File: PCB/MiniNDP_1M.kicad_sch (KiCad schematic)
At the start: 18 parts, among them J1 Conn_02x20_Odd_Even, U1 HC161, U2 HC161, U3 HC161, U4 HC138, U5 FCT821, U6 AS6C8008_TSOPII, U7 1G32

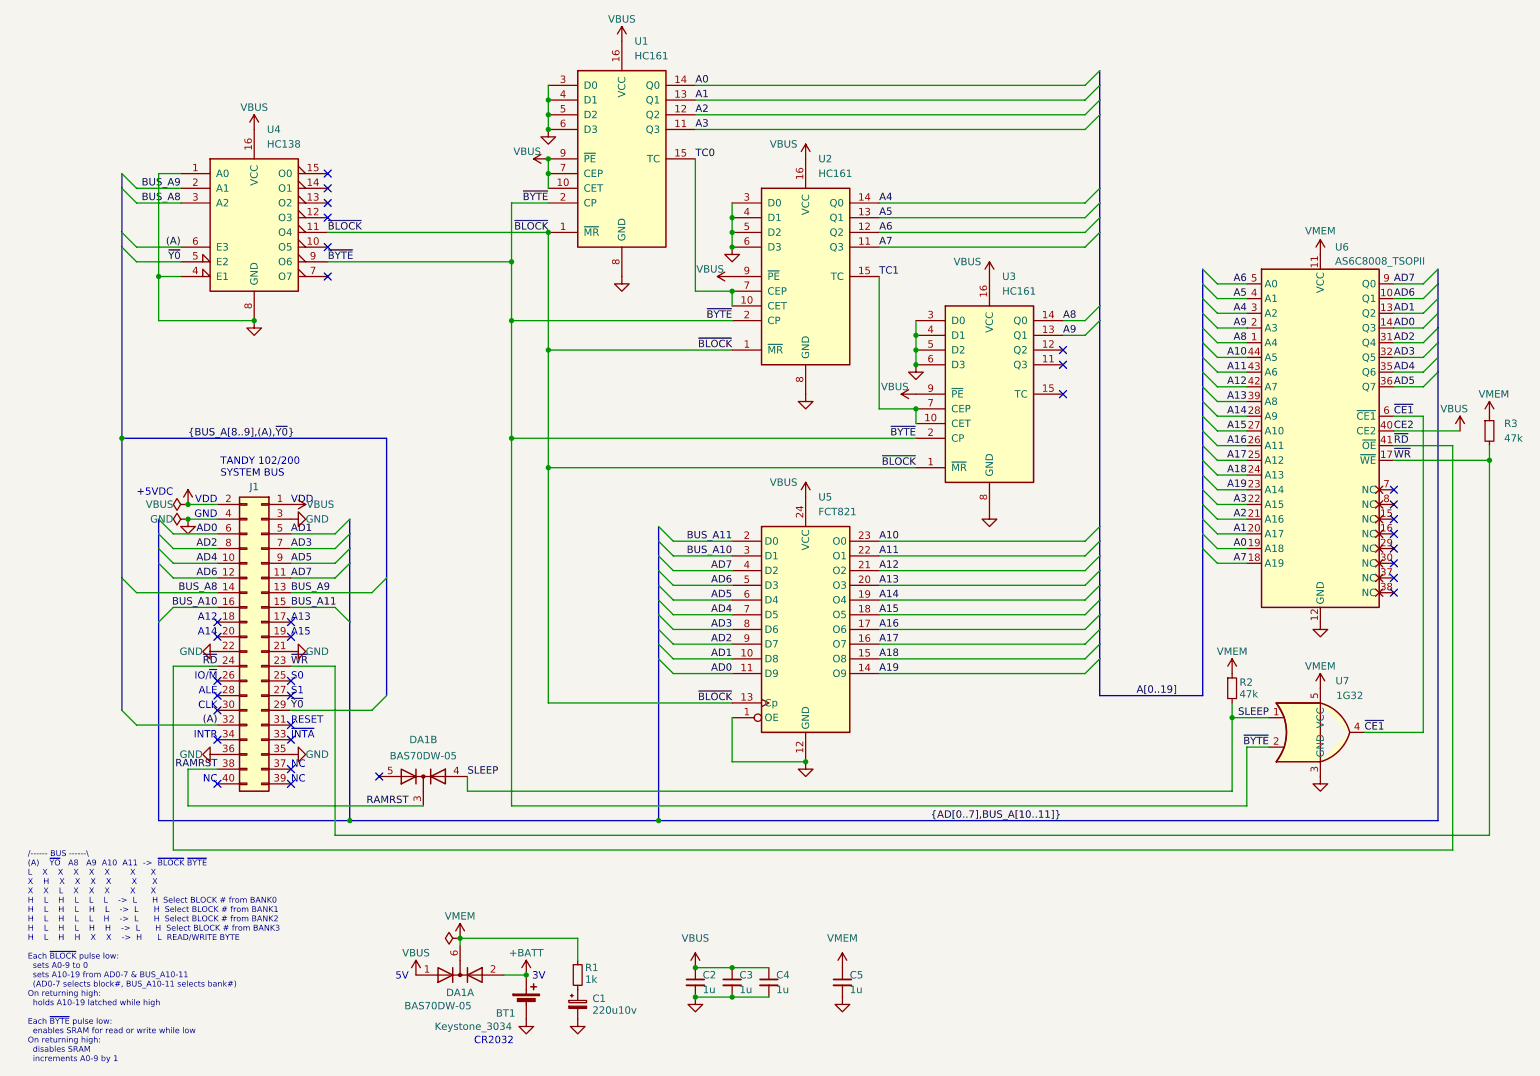
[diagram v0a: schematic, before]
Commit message: Add pullup on /WR. Tighter cover fit.
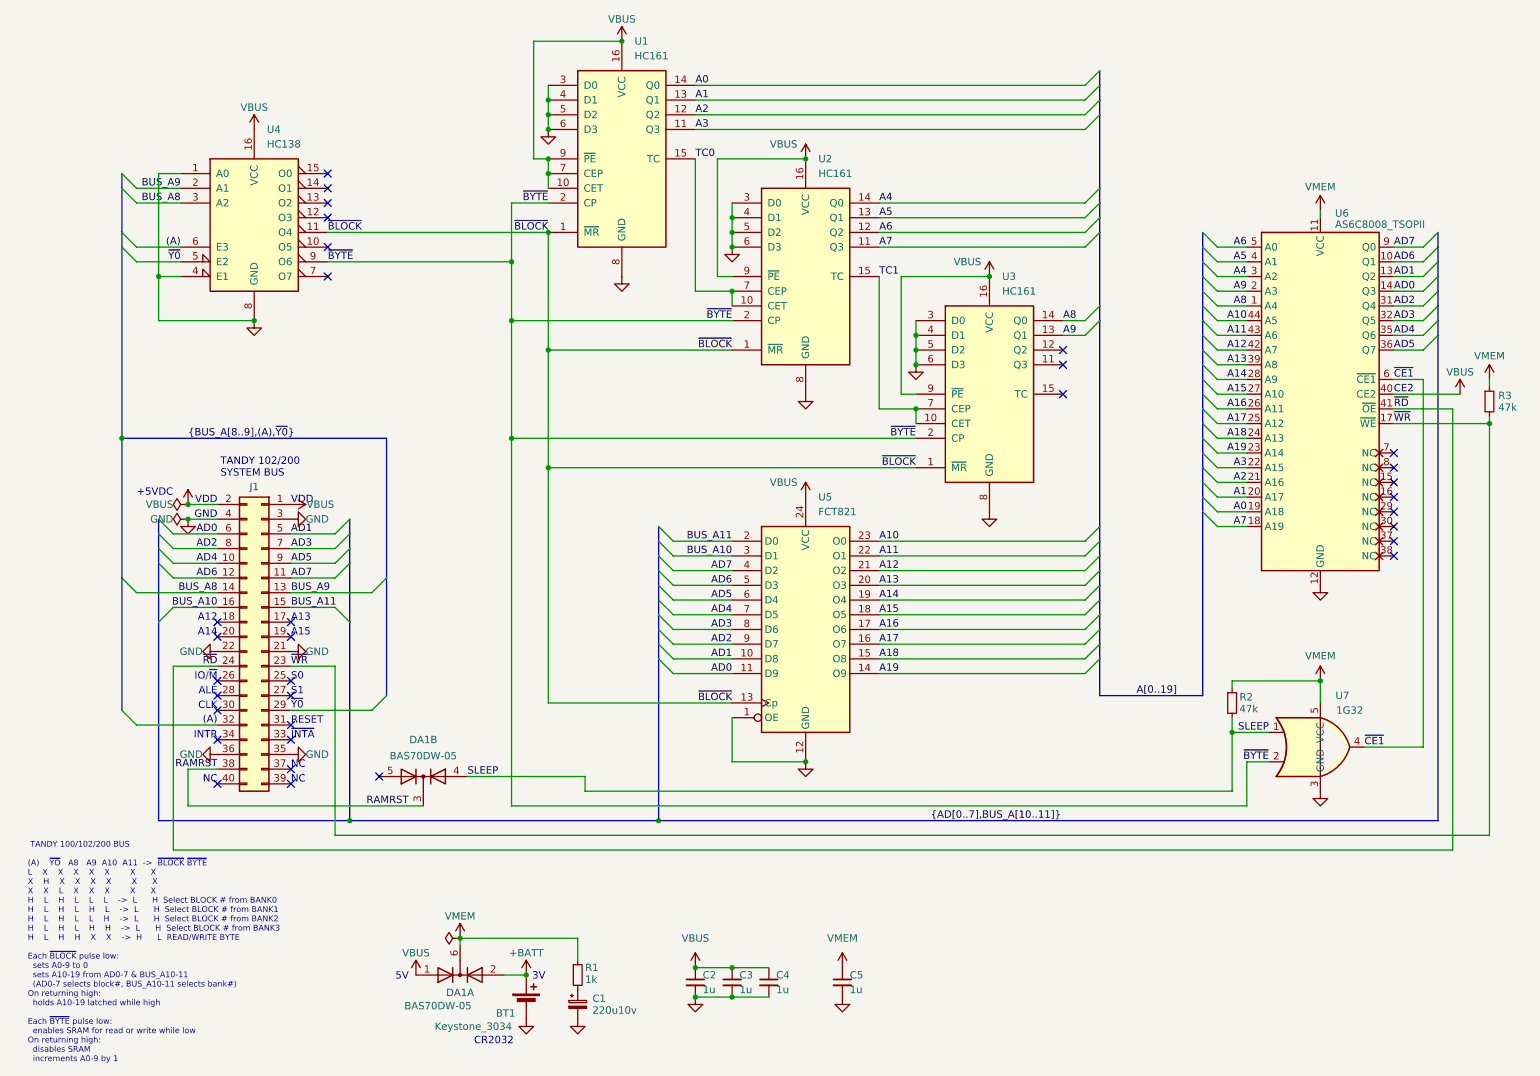
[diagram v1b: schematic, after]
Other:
- note added: "TANDY 100/102/200 BUS (A) ~{YO} A8 A9 A10 A11 -> ~{BLOCK} ~{BYTE} L X X X X X X X X H X X X X X X X X L X X X X X H L H L L L -> L H Select BLOCK # from BANK0 H L H L H L -> L H Select BLOCK # from BANK1 H L H L L H -> L H Select BLOCK # from BANK2 H L H L H H -> L H Select BLOCK # from BANK3 H L H H X X -> H L READ/WRITE BYTE Each ~{BLOCK} pulse low: sets A0-9 to 0 sets A10-19 from AD0-7 & BUS_A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"
- note removed: "/------ BUS ------\ (A) ~{YO} A8 A9 A10 A11 -> ~{BLOCK} ~{BYTE} L X X X X X X X X H X X X X X X X X L X X X X X H L H L L L -> L H Select BLOCK # from BANK0 H L H L H L -> L H Select BLOCK # from BANK1 H L H L L H -> L H Select BLOCK # from BANK2 H L H L H H -> L H Select BLOCK # from BANK3 H L H H X X -> H L READ/WRITE BYTE Each ~{BLOCK} pulse low: sets A0-9 to 0 sets A10-19 from AD0-7 & BUS_A10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"
- moved on the sheet: R2, R3, U6, U7

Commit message: 512_E & 1M silkscreen, MPNs in sch, pos & bom
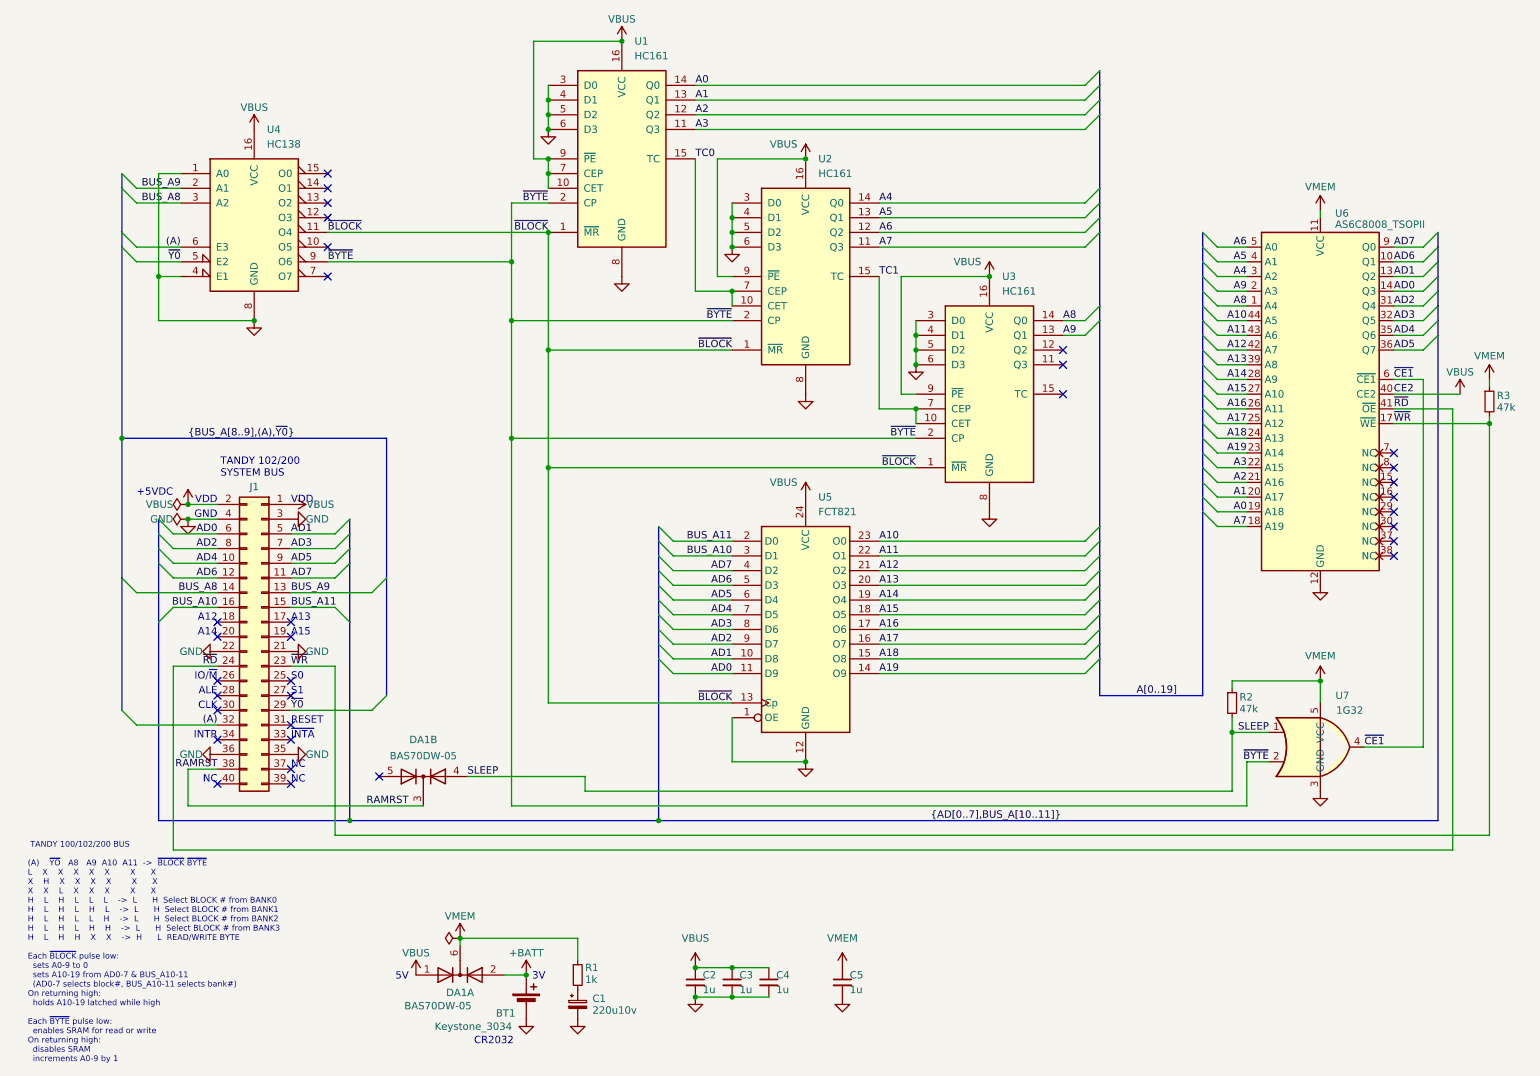
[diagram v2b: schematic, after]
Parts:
- BT1: MPN (none) -> Keystone 3034
- C1: MPN (none) -> TAJC227K010RNJ
- C2, C3, C4, C5: MPN (none) -> CL21B105KAFNNNE
- DA1: MPN (none) -> BAS70DW-05-7-F
- J1: MPN (none) -> 302-S401
- R1: MPN (none) -> RK73B2ATTD102J
- R2, R3: MPN (none) -> RMCF0805FT47K0
- U1, U2, U3: MPN (none) -> 74HC161PW,118
- U4: MPN (none) -> 74HC138PW,118
- U5: MPN (none) -> CY74FCT821BTSOC
- U6: MPN (none) -> AS6C8008-55ZIN
- U7: MPN (none) -> 74LVC1G32GW,125

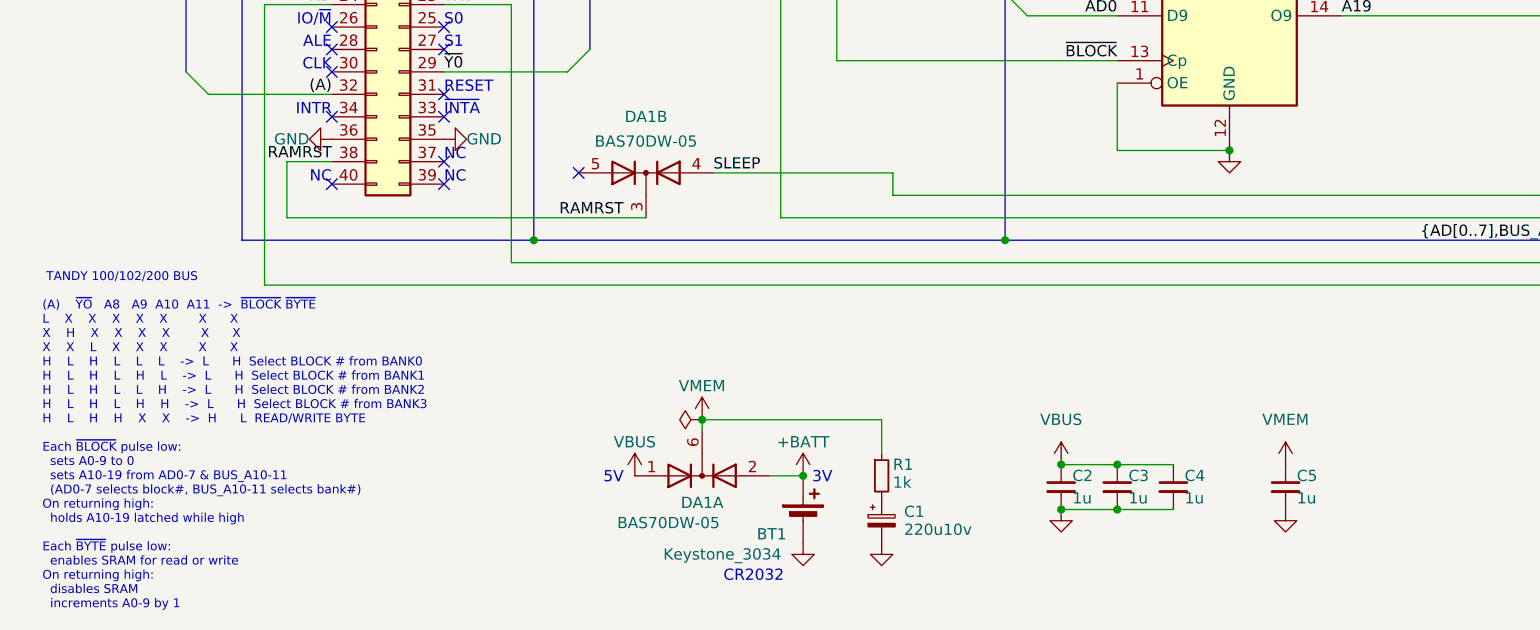
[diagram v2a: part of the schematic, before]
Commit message: make E version default, easier to solder
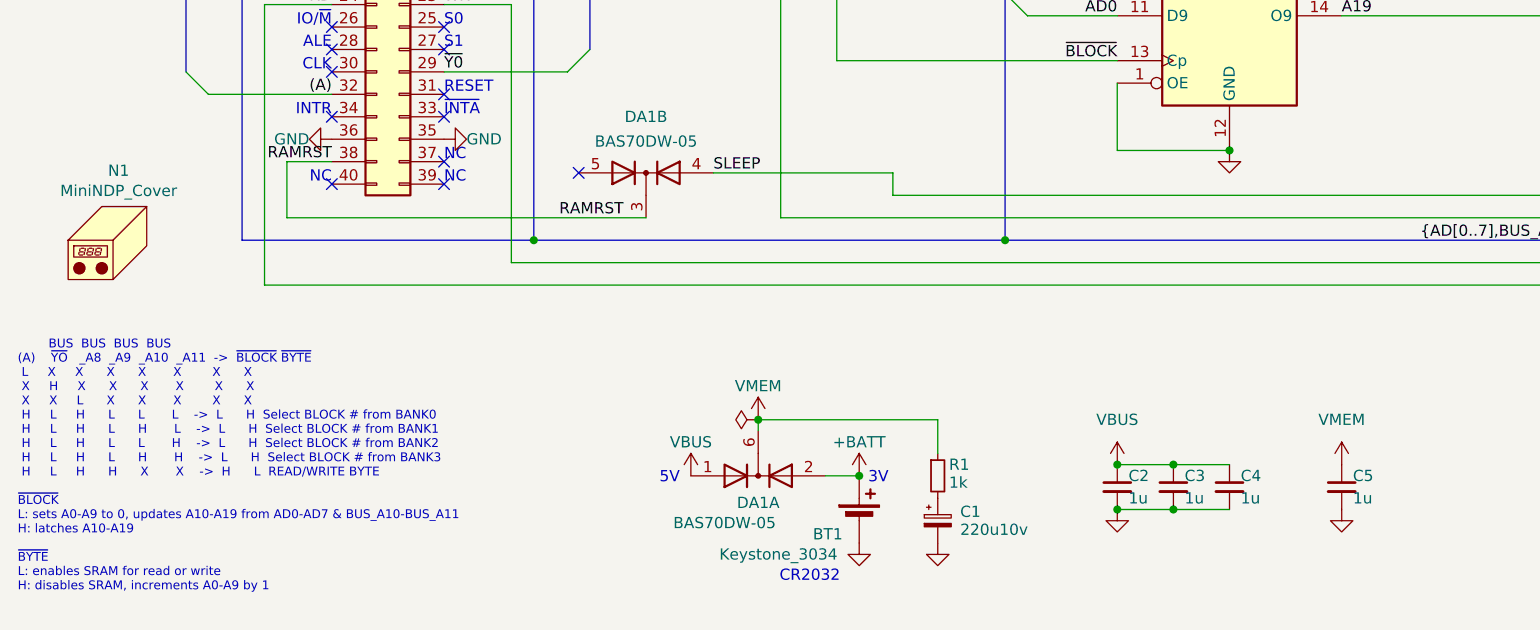
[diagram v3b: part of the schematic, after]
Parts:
- added N1: MiniNDP_Cover, 000_LOCAL:MiniNDP_Cover, symbol 000_LOCAL:Housing
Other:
- note added: "BUS BUS BUS BUS (A) ~{YO} _A8 _A9 _A10 _A11 -> ~{BLOCK} ~{BYTE} L X X X X X X X X H X X X X X X X X L X X X X X H L H L L L -> L H Select BLOCK # from BANK0 H L H L H L -> L H Select BLOCK # from BANK1 H L H L L H -> L H Select BLOCK # from BANK2 H L H L H H -> L H Select BLOCK # from BANK3 H L H H X X -> H L READ/WRITE BYTE ~{BLOCK} L: sets A0-A9 to 0, updates A10-A19 from AD0-AD7 & BUS_A10-BUS_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"
- note removed: "TANDY 100/102/200 BUS (A) ~{YO} A8 A9 A10 A11 -> ~{BLOCK} ~{BYTE} L X X X X X X X X H X X X X X X X X L X X X X X H L H L L L -> L H Select BLOCK # from BANK0 H L H L H L -> L H Select BLOCK # from BANK1 H L H L L H -> L H Select BLOCK # from BANK2 H L H L H H -> L H Select BLOCK # from BANK3 H L H H X X -> H L READ/WRITE BYTE Each ~{BLOCK} pulse low: sets A0-9 to 0 sets A10-19 from AD0-7 & BUS_A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"
- moved on the sheet: BT1, C1, C2, C3, C4, C5, DA1A, R1
